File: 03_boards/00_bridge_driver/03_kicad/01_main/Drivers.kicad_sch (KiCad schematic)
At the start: 42 parts, among them Q1 SUD90330E, Q2 SUD90330E, Q3 SUD90330E, Q4 SUD90330E, Q5 SUD90330E, Q6 SUD90330E, U1 IRS2104, U2 IRS2104, U3 IRS2104

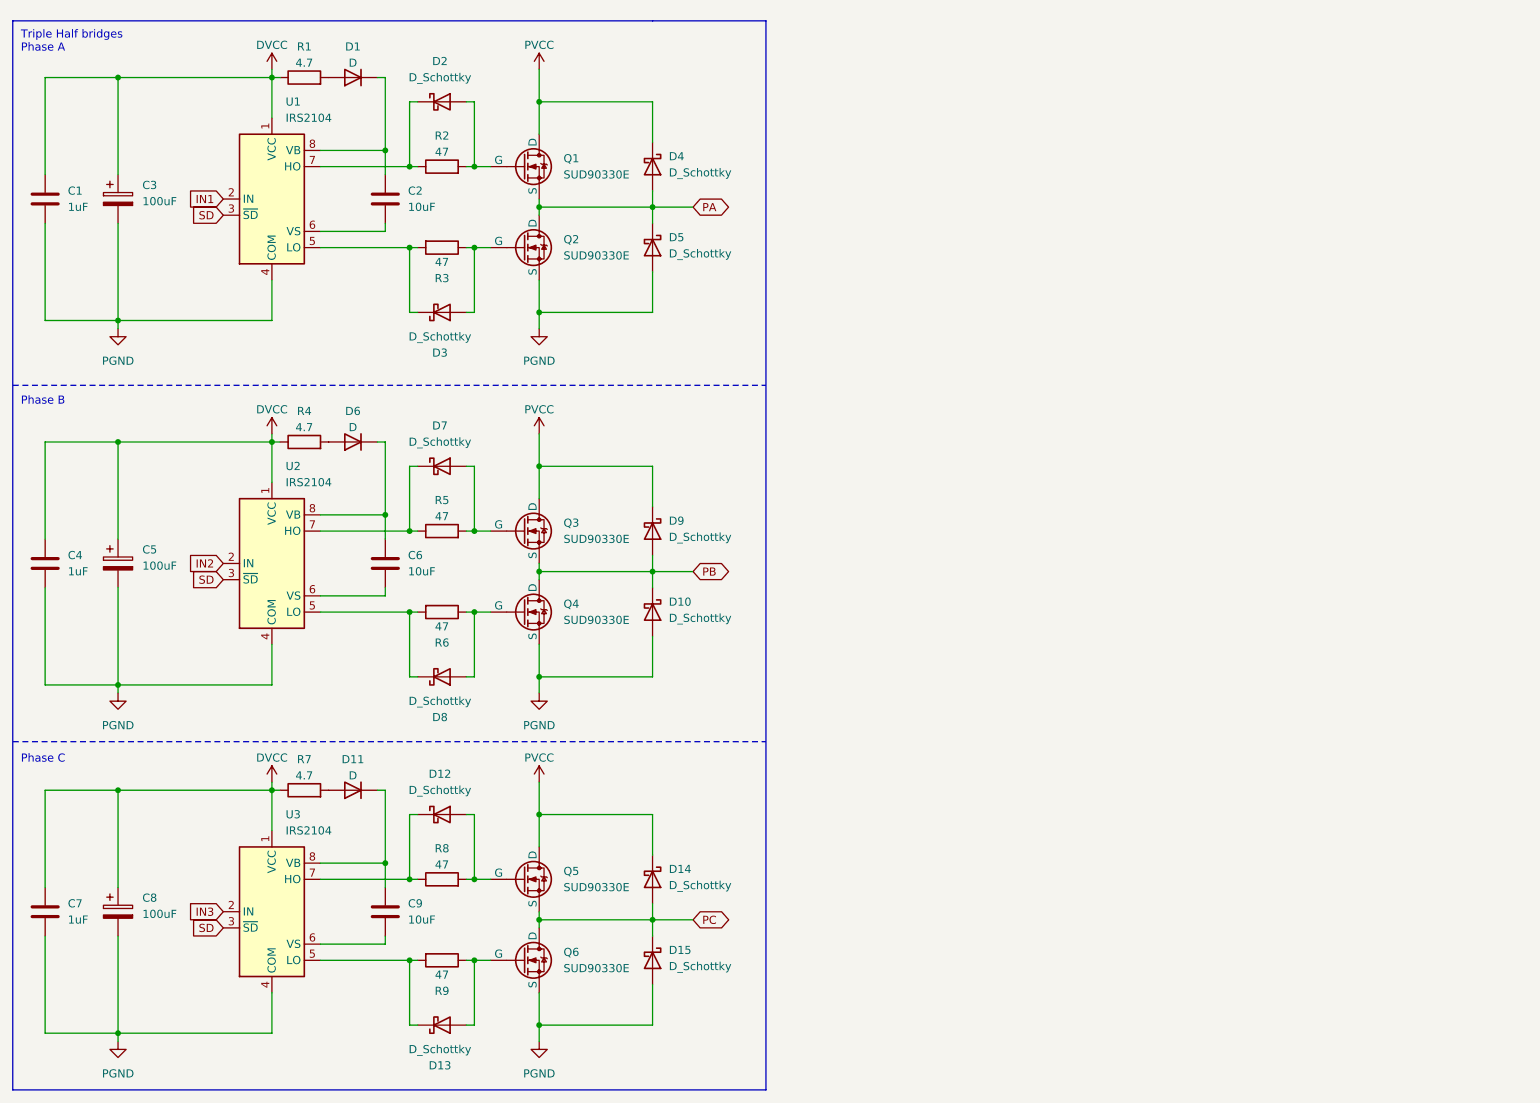
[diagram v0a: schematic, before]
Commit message: Few changes to the model model & Selected Boot Diodes
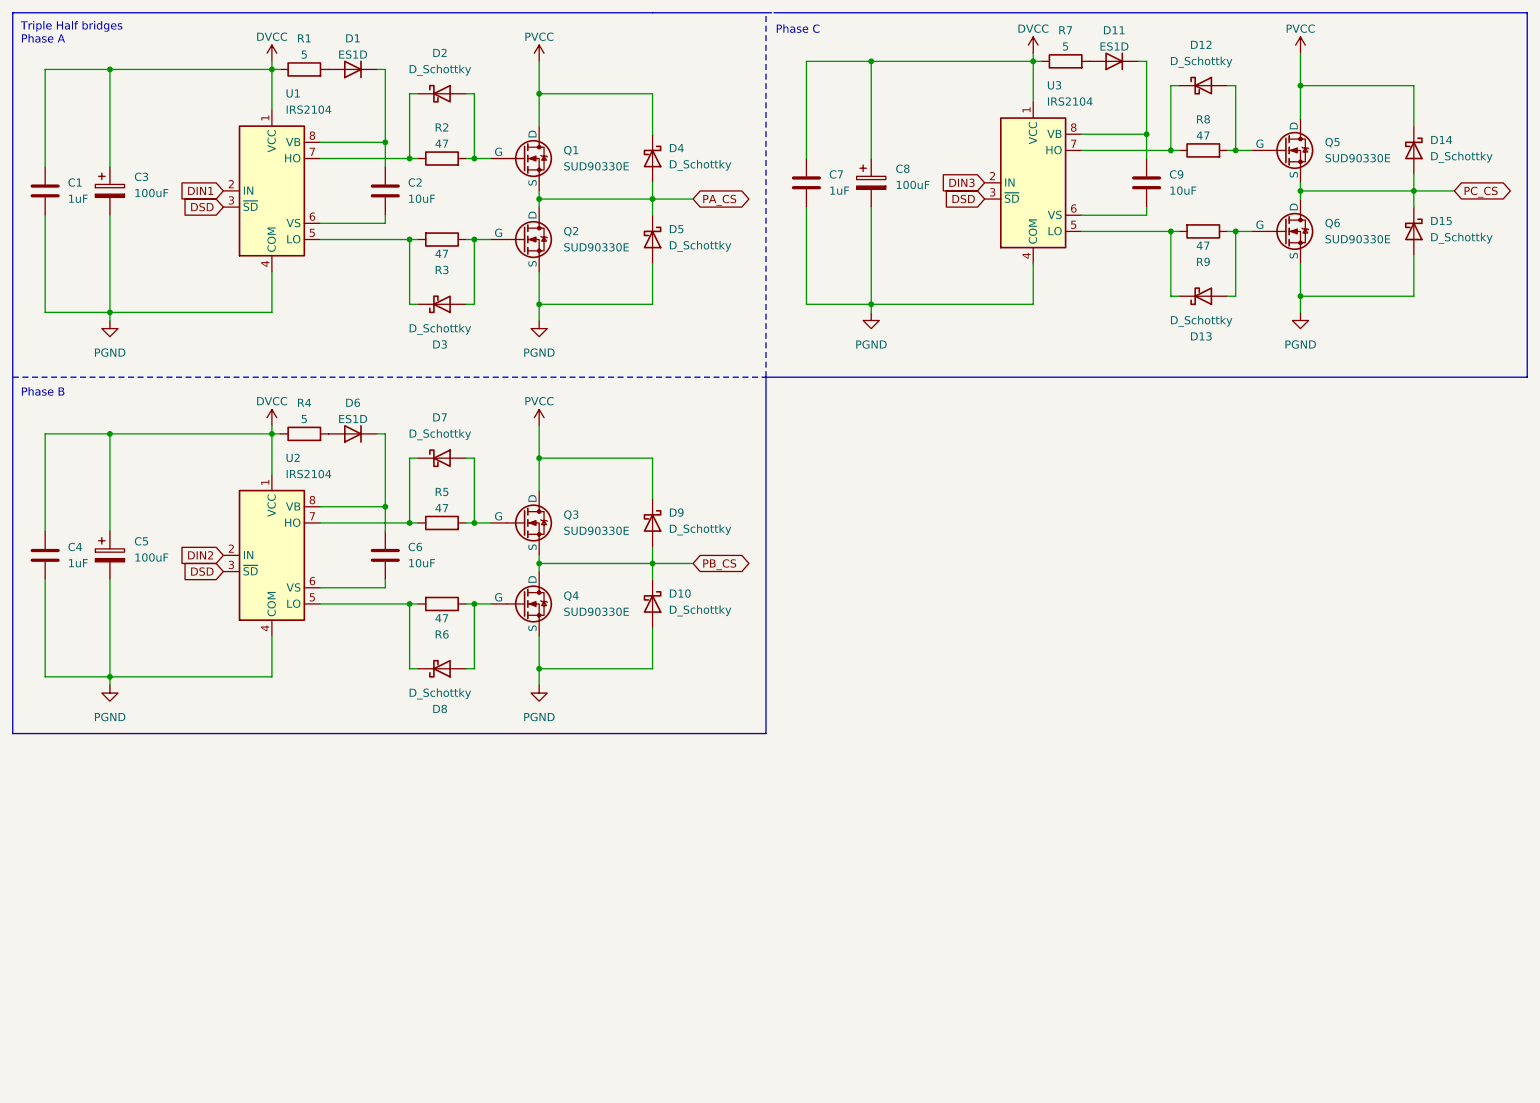
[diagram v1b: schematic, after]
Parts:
- D1, D11, D6: value D -> ES1D
- R1, R4, R7: value 4.7 -> 5
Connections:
- net IN1 renamed DIN1
- net IN2 renamed DIN2
- net IN3 renamed DIN3
- net PA renamed PA_CS
- net PB renamed PB_CS
- net PC renamed PC_CS
- net SD renamed DSD
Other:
- title: Triple half bridge drivers and switches -> (none)

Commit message: Triple bridge driver layout
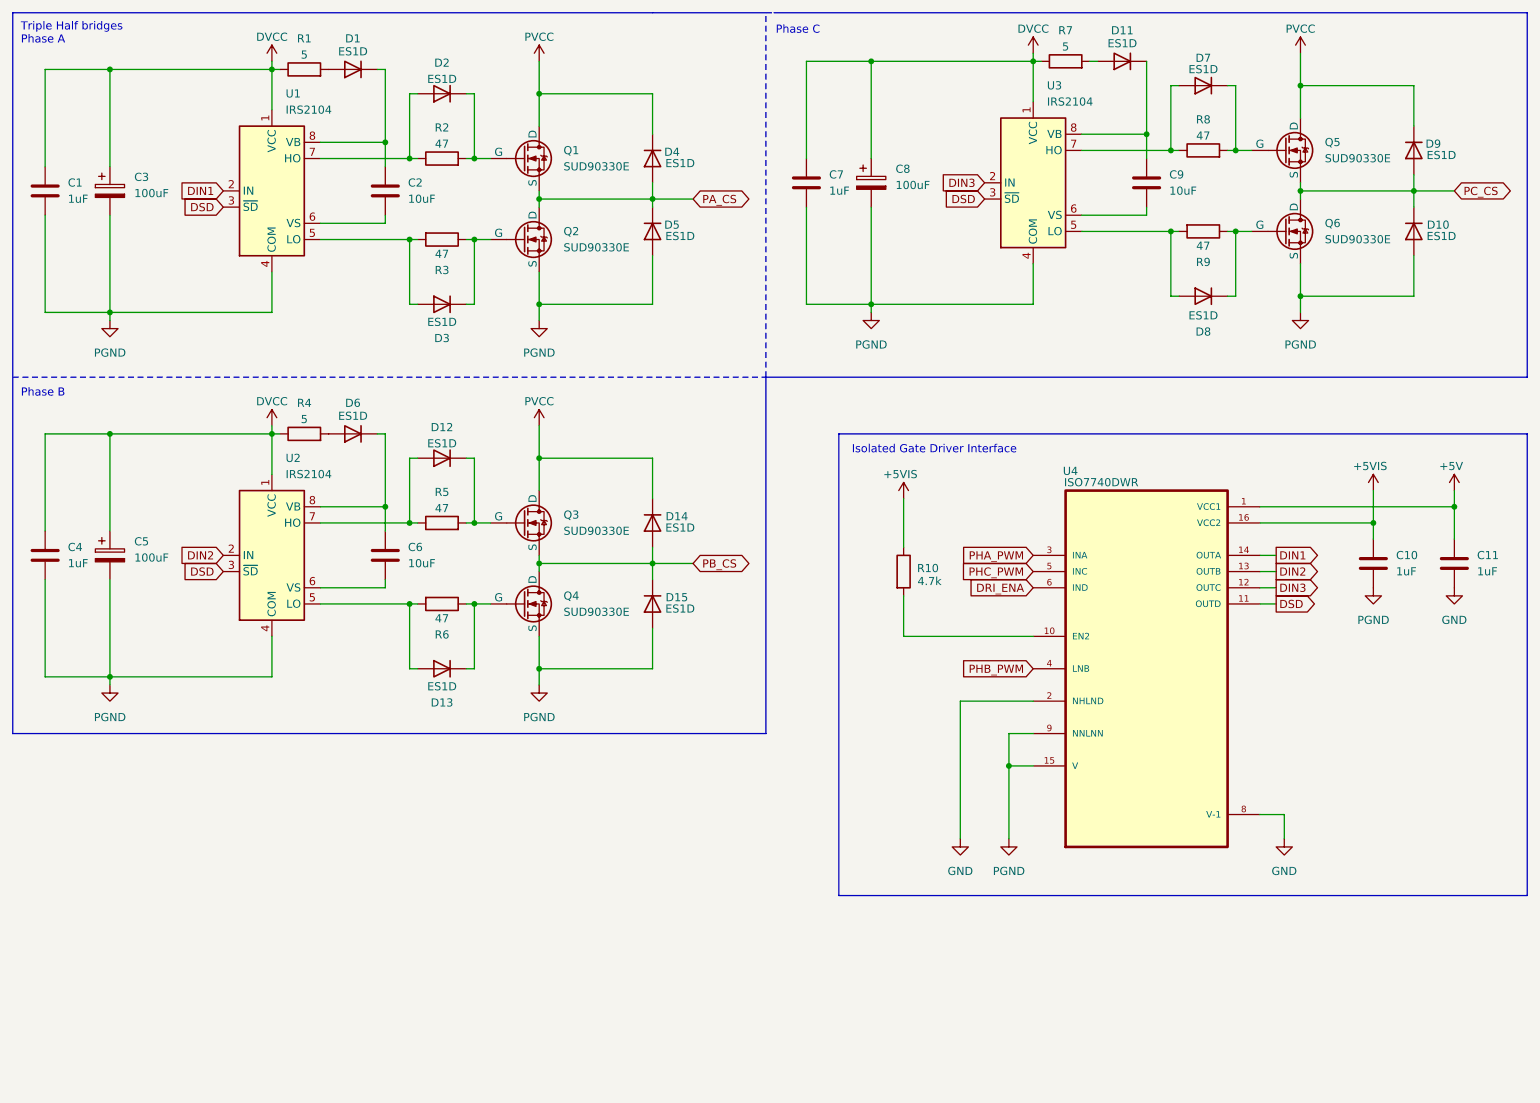
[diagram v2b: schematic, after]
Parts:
- removed D10, D12, D13, D14, D15, D2, D3, D4, D5, D7, D8, D9: D_Schottky, symbol Device:D_Schottky
- added C10, C11: 1uF, symbol Device:C
- added D10, D12, D13, D14, D15, D2, D3, D4, D5, D7, D8, D9: ES1D, symbol Device:D
- added R10: 4.7k, symbol Device:R
- added U4: ISO7740DWR, ISO7740DWR:SOIC127P1030X265-16N, symbol 2026-07-25_11-21-53:ISO7740DWR
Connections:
- net DIN1: now also U4.14 (OUTA)
- net DIN2: now also U4.13 (OUTB)
- net DIN3: now also U4.12 (OUTC)
- net DSD: now also U4.11 (OUTD)
- net PA_CS: now also D4.2 (A), D5.1 (K)
- net PB_CS: now also D14.2 (A), D15.1 (K)
- net PC_CS: now also D10.1 (K), D9.2 (A)
- net PGND: now also C10.2, D10.2 (A), D15.2 (A), D5.2 (A), U4.15 (V), U4.9 (NNLNN)
- net PVCC: now also D14.1 (K), D4.1 (K), D9.1 (K)
- net at Q5.2 (G), R8.2: now also D7.1 (K)
- net at R3.2, U1.5 (LO): now also D3.2 (A)
- net at R2.1, U1.7 (HO): now also D2.2 (A)
- net at Q1.2 (G), R2.2: now also D2.1 (K)
- net at R8.1, U3.7 (HO): now also D7.2 (A)
- net at R5.1, U2.7 (HO): now also D12.2 (A)
- net at Q3.2 (G), R5.2: now also D12.1 (K)
- net at R6.2, U2.5 (LO): now also D13.2 (A)
- net at Q4.2 (G), R6.1: now also D13.1 (K)
- net at Q2.2 (G), R3.1: now also D3.1 (K)
- net at R9.2, U3.5 (LO): now also D8.2 (A)
- net at Q6.2 (G), R9.1: now also D8.1 (K)
- new net: R10.2, U4.10 (EN2)
- new net +5V: C11.1, U4.1 (VCC1)
- new net +5VIS: C10.1, R10.1, U4.16 (VCC2)
- new net DRI_ENA: U4.6 (IND)
- new net GND: C11.2, U4.2 (NHLND), U4.8 (V-1)
- new net PHA_PWM: U4.3 (INA)
- new net PHB_PWM: U4.4 (LNB)
- new net PHC_PWM: U4.5 (INC)
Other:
- note added: "Isolated Gate Driver Interface"
- moved on the sheet: D11

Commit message: Updated the readmes a bit and moved the analytical to 00_analytical
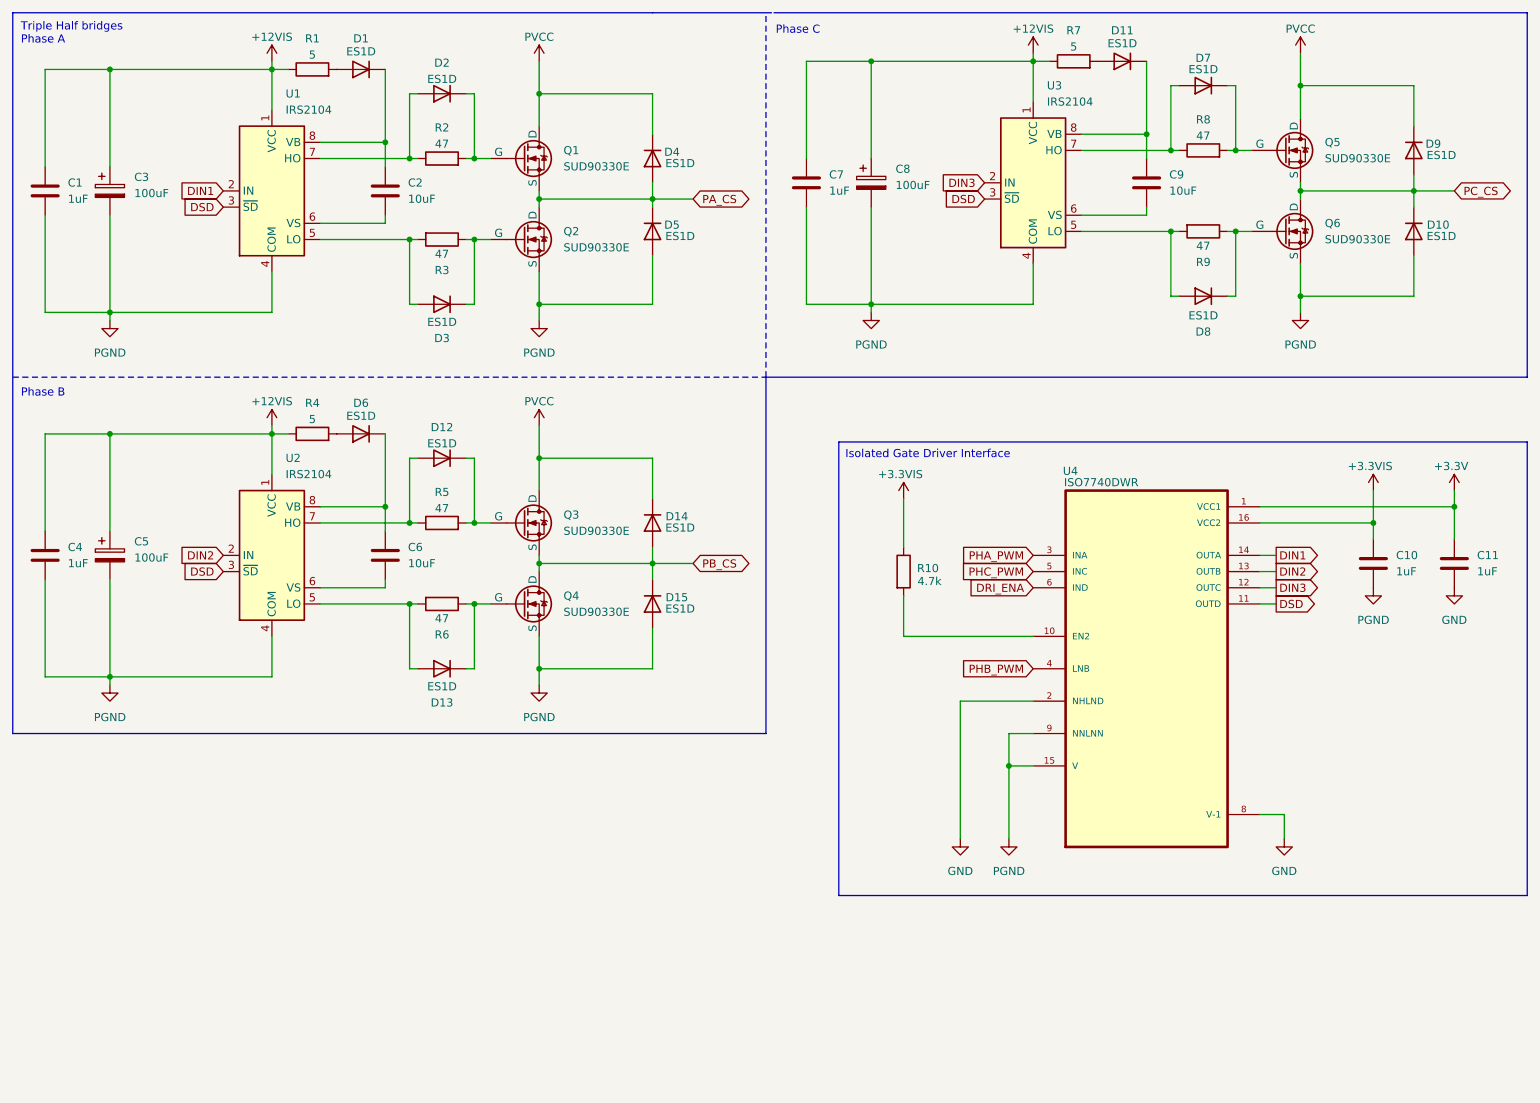
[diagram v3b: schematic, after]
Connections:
- net +5V renamed +3.3V
- net +5VIS renamed +3.3VIS
- net DVCC renamed +12VIS
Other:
- title: (none) -> Phase Drivers & Isolation
- moved on the sheet: D1, D6, R1, R4, R7
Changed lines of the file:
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@@
 	(generator_version "10.0")
 	(paper "A4")
+	(title_block
+		(title "Phase Drivers & Isolation")
+	)
 	(text "Isolated Gate Driver Interface\n"
 		(exclude_from_sim no)
-		(at 151.892 87.63 0)
+		(at 150.876 88.392 0)
 		(effects
 			(font
@@
 	(wire
 		(pts
-			(xy 60.96 27.94) (xy 62.23 27.94)
+			(xy 60.96 27.94) (xy 63.5 27.94)
 		)
 		(stroke
@@
 	(wire
 		(pts
-			(xy 78.74 85.09) (xy 77.47 85.09)
-		)
-		(stroke
-			(width 0)
-			(type default)
-		)
-	)
-	(wire
-		(pts
 			(xy 25.4 107.95) (xy 25.4 123.19)
 		)
@@
 	(polyline
 		(pts
-			(xy 257.81 85.09) (xy 257.81 157.48)
+			(xy 257.81 86.36) (xy 257.81 157.48)
 		)
 		(stroke
@@
 	(polyline
 		(pts
-			(xy 149.86 85.09) (xy 149.86 157.48)
+			(xy 149.86 86.36) (xy 149.86 157.48)
 		)
 		(stroke
@@
 	(wire
 		(pts
-			(xy 78.74 27.94) (xy 77.47 27.94)
-		)
-		(stroke
-			(width 0)
-			(type default)
-		)
-	)
-	(wire
-		(pts
 			(xy 120.65 88.9) (xy 102.87 88.9)
 		)
@@
 	(polyline
 		(pts
-			(xy 149.86 85.09) (xy 257.81 85.09)
+			(xy 149.86 86.36) (xy 257.81 86.36)
 		)
 		(stroke
@@
 	(wire
 		(pts
-			(xy 60.96 85.09) (xy 62.23 85.09)
+			(xy 60.96 85.09) (xy 63.5 85.09)
 		)
 		(stroke
@@
 	(wire
 		(pts
-			(xy 180.34 26.67) (xy 181.61 26.67)
+			(xy 180.34 26.67) (xy 182.88 26.67)
 		)
 		(stroke
@@
 	(wire
 		(pts
-			(xy 190.5 26.67) (xy 189.23 26.67)
-		)
-		(stroke
-			(width 0)
-			(type default)
-		)
-	)
-	(wire
-		(pts
 			(xy 187.96 40.64) (xy 201.93 40.64)
 		)
@@
 	(symbol
 		(lib_id "Device:R")
-		(at 185.42 26.67 90)
+		(at 186.69 26.67 90)
 		(unit 1)
 		(body_style 1)
@@
 		(dnp no)
 		(property "Reference" "R7"
-			(at 185.42 21.844 90)
+			(at 186.69 21.844 90)
 			(show_name no)
 			(do_not_autoplace no)
@@
 		)
 		(property "Value" "5"
-			(at 185.42 24.384 90)
+			(at 186.69 24.384 90)
 			(show_name no)
 			(do_not_autoplace no)
@@
 		)
 		(property "Footprint" ""
-			(at 185.42 28.448 90)
+			(at 186.69 28.448 90)
 			(hide yes)
 			(show_name no)
@@
 		)
 		(property "Datasheet" ""
-			(at 185.42 26.67 0)
+			(at 186.69 26.67 0)
 			(hide yes)
 			(show_name no)
@@
 		)
 		(property "Description" "Resistor"
-			(at 185.42 26.67 0)
+			(at 186.69 26.67 0)
 			(hide yes)
 			(show_name no)
@@
 			)
 		)
-		(property "Value" "+5VIS"
+		(property "Value" "+3.3VIS"
 			(at 159.512 91.44 0)
 			(show_name no)
@@
 			)
 		)
-		(property "Value" "DVCC"
+		(property "Value" "+12VIS"
 			(at 60.96 22.86 0)
 			(show_name no)
@@
 			)
 		)
-		(property "Value" "DVCC"
+		(property "Value" "+12VIS"
 			(at 60.96 80.01 0)
 			(show_name no)
@@
 	(symbol
 		(lib_id "Device:D")
-		(at 73.66 27.94 180)
+		(at 74.93 27.94 180)
 		(unit 1)
 		(body_style 1)
@@
 		(dnp no)
 		(property "Reference" "D1"
-			(at 73.66 23.114 0)
+			(at 74.93 23.114 0)
 			(show_name no)
 			(do_not_autoplace no)
@@
 		)
 		(property "Value" "ES1D"
-			(at 73.66 25.146 0)
+			(at 74.93 25.146 0)
 			(show_name no)
 			(do_not_autoplace no)
@@
 		)
 		(property "Footprint" ""
-			(at 73.66 27.94 0)
+			(at 74.93 27.94 0)
 			(hide yes)
 			(show_name no)
@@
 		)
 		(property "Datasheet" ""
-			(at 73.66 27.94 0)
+			(at 74.93 27.94 0)
 			(hide yes)
 			(show_name no)
@@
 		)
 		(property "Description" "Diode"
-			(at 73.66 27.94 0)
+			(at 74.93 27.94 0)
 			(hide yes)
 			(show_name no)
@@
 		)
 		(property "Sim.Device" "D"
-			(at 73.66 27.94 0)
+			(at 74.93 27.94 0)
 			(hide yes)
 			(show_name no)
@@
 		)
 		(property "Sim.Pins" "1=K 2=A"
-			(at 73.66 27.94 0)
+			(at 74.93 27.94 0)
 			(hide yes)
 			(show_name no)
@@
 	(symbol
 		(lib_id "Device:R")
-		(at 66.04 27.94 90)
+		(at 67.31 27.94 90)
 		(unit 1)
 		(body_style 1)
@@
 		(dnp no)
 		(property "Reference" "R1"
-			(at 66.04 23.114 90)
+			(at 67.31 23.114 90)
 			(show_name no)
 			(do_not_autoplace no)
@@
 		)
 		(property "Value" "5"
-			(at 66.04 25.654 90)
+			(at 67.31 25.654 90)
 			(show_name no)
 			(do_not_autoplace no)
@@
 		)
 		(property "Footprint" ""
-			(at 66.04 29.718 90)
+			(at 67.31 29.718 90)
 			(hide yes)
 			(show_name no)
@@
 		)
 		(property "Datasheet" ""
-			(at 66.04 27.94 0)
+			(at 67.31 27.94 0)
 			(hide yes)
 			(show_name no)
@@
 		)
 		(property "Description" "Resistor"
-			(at 66.04 27.94 0)
+			(at 67.31 27.94 0)
 			(hide yes)
 			(show_name no)
@@
 			)
 		)
-		(property "Value" "+5V"
+		(property "Value" "+3.3V"
 			(at 245.872 90.17 0)
 			(show_name no)
@@
 			)
 		)
-		(property "Value" "DVCC"
+		(property "Value" "+12VIS"
 			(at 180.34 21.59 0)
 			(show_name no)
@@
 	(symbol
 		(lib_id "Device:R")
-		(at 66.04 85.09 90)
+		(at 67.31 85.09 90)
 		(unit 1)
 		(body_style 1)
@@
 		(dnp no)
 		(property "Reference" "R4"
-			(at 66.04 80.264 90)
+			(at 67.31 80.264 90)
 			(show_name no)
 			(do_not_autoplace no)
@@
 		)
 		(property "Value" "5"
-			(at 66.04 82.804 90)
+			(at 67.31 82.804 90)
 			(show_name no)
 			(do_not_autoplace no)
@@
 		)
 		(property "Footprint" ""
-			(at 66.04 86.868 90)
+			(at 67.31 86.868 90)
 			(hide yes)
 			(show_name no)
@@
 		)
 		(property "Datasheet" ""
-			(at 66.04 85.09 0)
+			(at 67.31 85.09 0)
 			(hide yes)
 			(show_name no)
@@
 		)
 		(property "Description" "Resistor"
-			(at 66.04 85.09 0)
+			(at 67.31 85.09 0)
 			(hide yes)
 			(show_name no)
@@
 			)
 		)
-		(property "Value" "+5VIS"
+		(property "Value" "+3.3VIS"
 			(at 233.172 90.17 0)
 			(show_name no)
@@
 	(symbol
 		(lib_id "Device:D")
-		(at 73.66 85.09 180)
+		(at 74.93 85.09 180)
 		(unit 1)
 		(body_style 1)
@@
 		(dnp no)
 		(property "Reference" "D6"
-			(at 73.66 80.264 0)
+			(at 74.93 80.264 0)
 			(show_name no)
 			(do_not_autoplace no)
@@
 		)
 		(property "Value" "ES1D"
-			(at 73.66 82.296 0)
+			(at 74.93 82.296 0)
 			(show_name no)
 			(do_not_autoplace no)
@@
 		)
 		(property "Footprint" ""
-			(at 73.66 85.09 0)
+			(at 74.93 85.09 0)
 			(hide yes)
 			(show_name no)
@@
 		)
 		(property "Datasheet" ""
-			(at 73.66 85.09 0)
+			(at 74.93 85.09 0)
 			(hide yes)
 			(show_name no)
@@
 		)
 		(property "Description" "Diode"
-			(at 73.66 85.09 0)
+			(at 74.93 85.09 0)
 			(hide yes)
 			(show_name no)
@@
 		)
 		(property "Sim.Device" "D"
-			(at 73.66 85.09 0)
+			(at 74.93 85.09 0)
 			(hide yes)
 			(show_name no)
@@
 		)
 		(property "Sim.Pins" "1=K 2=A"
-			(at 73.66 85.09 0)
+			(at 74.93 85.09 0)
 			(hide yes)
 			(show_name no)
